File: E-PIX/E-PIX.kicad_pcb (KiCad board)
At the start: 2 copper layers, 40.1 x 45 mm, 65 parts, among them J1 USB_C_Receptacle_USB2.0, J2 DM3AT-SF-PEJM5, Q1 AO3401A, Q2 2SC4213, Q3 2SC4213, Q4 BSS138, Q5 BSS138, SW1 SW_Push, SW2 SW_Push, U10 ESP32-S3-WROOM-1, U2 NJM7805SDL1, U3 AZ1117-3.3, U4 BTS6142D, U5 Conn_03x02, U6 Conn_03x04, U7 U7, U8 U8, U9 FT231XS

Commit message: adjust all the footprints. start trying free routing
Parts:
- moved R14 1.27 mm to (140.2, 87.3)
- moved R19 1.27 mm to (144.0, 87.3)
- moved R4 1.27 mm to (147.8, 87.3)
- renumbered U1 to BNO055
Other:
- board text added: "CPU"
- board text added: "POWER"
- board text added: "VSS"
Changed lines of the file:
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@@
 		(tags "capacitor")
 		(property "Reference" "C11"
-			(at -1.7 1.905 180)
+			(at -1.7 2.54 180)
 			(layer "F.SilkS")
 			(effects
@@
 		(tags "USB C Type-C Receptacle SMD")
 		(property "Reference" "J1"
-			(at 4.57 -5.715 90)
+			(at 0.125 -5.715 90)
 			(layer "F.SilkS")
 			(effects
@@
 		(descr "PH-3X4SG")
 		(property "Reference" "U6"
-			(at -3.81 -1.27 0)
+			(at -3.175 -1.27 0)
 			(layer "F.SilkS")
 			(effects
@@
 		(tags "SSOP 0.635")
 		(property "Reference" "U9"
-			(at 5.02 -3.4925 180)
+			(at 3.75 -4.1275 180)
 			(layer "F.SilkS")
 			(effects
@@
 		(tags "DPAK TO-252 DPAK-5 TO-252-5")
 		(property "Reference" "U4"
-			(at -4.86 -0.001 90)
+			(at 2.76 4.825 0)
 			(layer "F.SilkS")
 			(effects
@@
 		(descr "PH-3X4SG")
 		(property "Reference" "U5"
-			(at -1.905 5.715 90)
+			(at -2.54 5.715 90)
 			(layer "F.SilkS")
 			(effects
@@
 		(tags "CP Radial series Radial pin pitch 3.50mm diameter 8mm height 12mm Electrolytic Capacitor")
 		(property "Reference" "C3"
-			(at 1.75 5.08 90)
+			(at -3.81 2.54 90)
 			(layer "F.SilkS")
 			(effects
@@
 		(tags "LED")
 		(property "Reference" "D9"
-			(at -3.0225 0 90)
+			(at 1.38 4.76 180)
 			(layer "B.SilkS")
 			(effects
 				(font
-					(size 1 1)
-					(thickness 0.15)
+					(size 0.6 0.6)
+					(thickness 0.075)
 				)
 				(justify mirror)
@@
 		(property "Value" "U7"
 			(at 1.85 0.026 0)
-			(layer "B.SilkS")
+			(layer "B.SilkS" knockout)
 			(effects
 				(font
 					(size 1 1)
-					(thickness 0.2)
+					(thickness 0.15)
 				)
 				(justify mirror)
@@
 		(layer "B.Cu")
 		(at 131.75 91.11 180)
-		(property "Reference" "U1"
-			(at 0 13 0)
+		(property "Reference" "BNO055"
+			(at 0 -10.16 0)
 			(unlocked yes)
 			(layer "B.SilkS")
@@
 				(font
 					(size 1 1)
-					(thickness 0.1)
+					(thickness 0.15)
 				)
 				(justify mirror)
@@
 		(tags "capacitor")
 		(property "Reference" "C7"
-			(at 2.225 0 90)
+			(at 1.59 0 90)
 			(layer "B.SilkS")
 			(effects
 				(font
-					(size 1 1)
-					(thickness 0.15)
+					(size 0.6 0.6)
+					(thickness 0.075)
 				)
 				(justify mirror)
@@
 		(tags "capacitor")
 		(property "Reference" "C9"
-			(at 3.315 0 90)
+			(at 1.05558 -1.905 180)
 			(layer "B.SilkS")
 			(effects
 				(font
-					(size 1 1)
-					(thickness 0.15)
+					(size 0.6 0.6)
+					(thickness 0.075)
 				)
 				(justify mirror)
@@
 	(footprint "Resistor_SMD:R_0603_1608Metric"
 		(layer "B.Cu")
-		(at 145.275 87.3 180)
+		(at 144.005 87.3 180)
 		(descr "Resistor SMD 0603 (1608 Metric), square (rectangular) end terminal, IPC-7351 nominal, (Body size source: IPC-SM-782 page 72, https://www.pcb-3d.com/wordpress/wp-content/uploads/ipc-sm-782a_amendment_1_and_2.pdf), generated with kicad-footprint-generator")
 		(tags "resistor")
 		(property "Reference" "R19"
-			(at 0 1.43 0)
+			(at 4.635 -2.54 0)
 			(layer "B.SilkS")
 			(effects
 				(font
-					(size 1 1)
-					(thickness 0.15)
+					(size 0.6 0.6)
+					(thickness 0.075)
 				)
 				(justify mirror)
@@
 		(tags "capacitor")
 		(property "Reference" "C8"
-			(at 2.225 0 90)
+			(at 1.59 0 90)
 			(layer "B.SilkS")
 			(effects
 				(font
-					(size 1 1)
-					(thickness 0.15)
+					(size 0.6 0.6)
+					(thickness 0.075)
 				)
 				(justify mirror)
@@
 		(tags "LED")
 		(property "Reference" "D4"
-			(at -3.0225 0 270)
+			(at -1.16 7.3 0)
 			(layer "B.SilkS")
 			(effects
 				(font
-					(size 1 1)
-					(thickness 0.15)
+					(size 0.6 0.6)
+					(thickness 0.075)
 				)
 				(justify mirror)
@@
 		(tags "capacitor")
 		(property "Reference" "C10"
-			(at 3.315 0 90)
+			(at 0.14 -4.445 180)
 			(layer "B.SilkS")
 			(effects
 				(font
-					(size 1 1)
-					(thickness 0.15)
+					(size 0.6 0.6)
+					(thickness 0.075)
 				)
 				(justify mirror)
@@
 		(tags "resistor")
 		(property "Reference" "R15"
-			(at 3.315 0 90)
+			(at 0.14 1.905 90)
 			(layer "B.SilkS")
 			(effects
@@
 	(footprint "Resistor_SMD:R_0603_1608Metric"
 		(layer "B.Cu")
-		(at 149.085 87.3 180)
+		(at 147.815 87.3 180)
 		(descr "Resistor SMD 0603 (1608 Metric), square (rectangular) end terminal, IPC-7351 nominal, (Body size source: IPC-SM-782 page 72, https://www.pcb-3d.com/wordpress/wp-content/uploads/ipc-sm-782a_amendment_1_and_2.pdf), generated with kicad-footprint-generator")
 		(tags "resistor")
 		(property "Reference" "R4"
-			(at 0 1.43 0)
+			(at 8.445 -1.27 0)
 			(layer "B.SilkS")
 			(effects
 				(font
-					(size 1 1)
-					(thickness 0.15)
+					(size 0.6 0.6)
+					(thickness 0.075)
 				)
 				(justify mirror)
@@
 	(footprint "Resistor_SMD:R_0603_1608Metric"
 		(layer "B.Cu")
-		(at 141.465 87.3 180)
+		(at 140.195 87.3 180)
 		(descr "Resistor SMD 0603 (1608 Metric), square (rectangular) end terminal, IPC-7351 nominal, (Body size source: IPC-SM-782 page 72, https://www.pcb-3d.com/wordpress/wp-content/uploads/ipc-sm-782a_amendment_1_and_2.pdf), generated with kicad-footprint-generator")
 		(tags "resistor")
 		(property "Reference" "R14"
-			(at 0 1.43 0)
+			(at 0.825 -3.81 0)
 			(layer "B.SilkS")
 			(effects
 				(font
-					(size 1 1)
-					(thickness 0.15)
+					(size 0.6 0.6)
+					(thickness 0.075)
 				)
 				(justify mirror)
@@
 				(font
 					(size 1 1)
-					(thickness 0.2)
+					(thickness 0.15)
 				)
 				(justify mirror)
@@
 		(tags "LED RGB NeoPixel PLCC-4 5050")
 		(property "Reference" "D6"
-			(at 4.765 0.125 0)
+			(at -4.76 2.03 0)
 			(layer "B.SilkS")
 			(effects
@@
 			(layer "B.Fab")
 		)
-		(fp_text user "1"
-			(at -4.15 1.6 0)
-			(layer "B.SilkS")
-			(effects
-				(font
-					(size 1 1)
-					(thickness 0.15)
-				)
-				(justify mirror)
-			)
-		)
 		(fp_text user "${REFERENCE}"
 			(at 0 0 0)
@@
 		(tags "LED")
 		(property "Reference" "D7"
-			(at -3.0225 0 90)
+			(at 0.11 2.22 180)
 			(layer "B.SilkS")
 			(effects
 				(font
-					(size 1 1)
-					(thickness 0.15)
+					(size 0.6 0.6)
+					(thickness 0.075)
 				)
 				(justify mirror)
@@
 		(layer "Edge.Cuts")
 	)
+	(gr_text "VSS"
+		(at 148.895 86.03 0)
+		(layer "B.SilkS")
+		(effects
+			(font
+				(size 0.6 0.6)
+				(thickness 0.075)
+			)
+			(justify left bottom mirror)
+		)
+	)
+	(gr_text "POWER"
+		(at 151.435 84.76 90)
+		(layer "B.SilkS")
+		(effects
+			(font
+				(size 1 1)
+				(thickness 0.15)
+			)
+			(justify left bottom mirror)
+		)
+	)
+	(gr_text "CPU"
+		(at 146.355 86.03 0)
+		(layer "B.SilkS")
+		(effects
+			(font
+				(size 0.6 0.6)
+				(thickness 0.075)
+			)
+			(justify left bottom mirror)
+		)
+	)
 	(embedded_fonts no)

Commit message: route main wires
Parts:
- R1: moved to F.Cu
- turned U9 to -90 degrees
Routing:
- net VSS: track 0.00 -> 41.2 mm, vias 0 -> 4
- net /ICS2_5V: track 0.00 -> 27.2 mm
- net /ICS1_5V: track 0.00 -> 17.8 mm
- net /CS: track 0.00 -> 16.9 mm, vias 0 -> 2
- net /MOSI: track 0.00 -> 15.4 mm, vias 0 -> 2
- net /CLK: track 0.00 -> 13.3 mm, vias 0 -> 2
- net /RX2: track 0.00 -> 12.4 mm, vias 0 -> 1
- net /TX2: track 0.00 -> 12.2 mm, vias 0 -> 1
- net /ICS2_3V3: track 0.00 -> 12.2 mm
- net /RX0: track 0.00 -> 11.9 mm
- net /ICS1_3V3: track 0.00 -> 11.7 mm
- net Net-(U4-IN): track 0.00 -> 10.8 mm
- net /MISO: track 0.00 -> 10.6 mm, vias 0 -> 2
- net /TX0: track 0.00 -> 10.0 mm
- net /TX1: track 0.00 -> 7.41 mm, vias 0 -> 1
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- added copper zone on F.Cu, net +3V3
- added copper zone on In1.Cu, net +3V3
- added copper zone on B.Cu, net GND
- added copper zone on F.Cu, net GND
- added copper zone on In1.Cu, net GND
- added copper zone on In2.Cu, net GND
- added copper zone on In3.Cu, net GND
- added copper zone on In4.Cu, net GND
- added copper zone on F.Cu, net VDD
- added copper zone on B.Cu, net VSS
- added copper zone on F.Cu, net VSS
- added copper zone on In1.Cu, net VSS
- added copper zone on In2.Cu, net VSS
- added copper zone on In3.Cu, net VSS
- added copper zone on In4.Cu, net VSS
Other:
- copper layers 2 -> 6

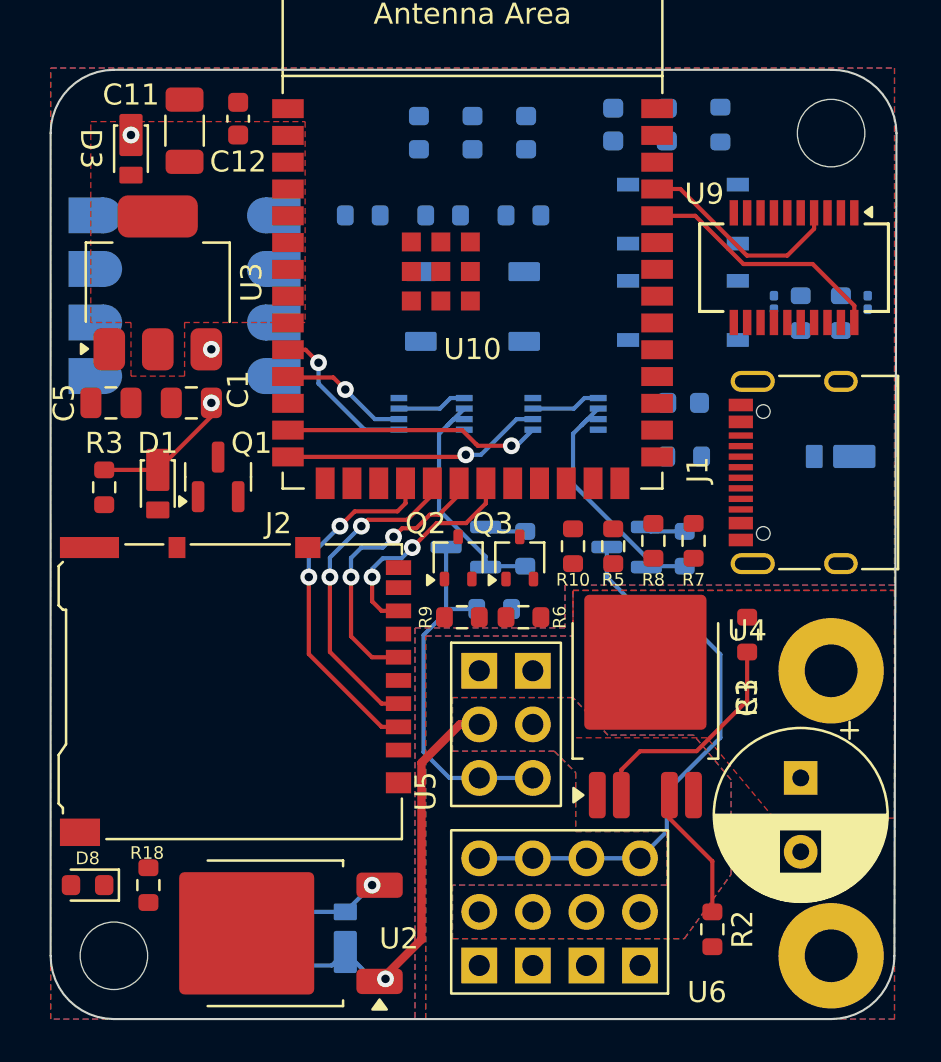
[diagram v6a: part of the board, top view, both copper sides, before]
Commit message: failed free routing
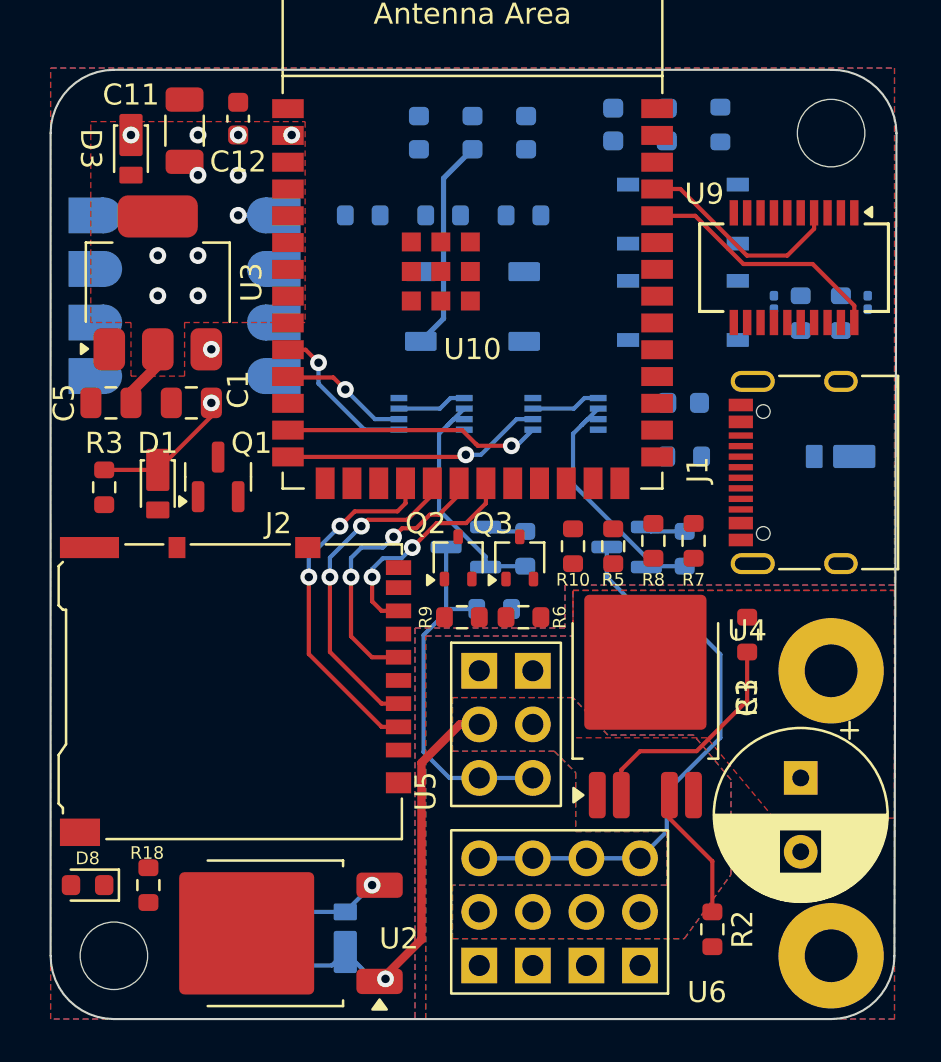
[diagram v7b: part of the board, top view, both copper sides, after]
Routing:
- net +3V3: track 3.87 -> 18.3 mm, vias 0 -> 10
- net VSS: track 41.2 -> 42.0 mm

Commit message: move some tips
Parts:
- C1, C5, D1, Q1, Q2, Q3, R10, R3, R5, R6, R7, R8, R9: moved to B.Cu
- C7, C8, Q4, Q5, R12, R13, R16, R17, R20, R21: moved to F.Cu
- U7: value U7 -> TC7WH241FK; moved to F.Cu
- U8: value U8 -> TC7WH241FK; moved to F.Cu
- moved R3 17.6 mm to (130.5, 82.7), turned to 0 degrees
- moved U8 17.6 mm to (132.4, 99.0), turned to 0 degrees
- moved U7 15.7 mm to (127.9, 99.0), turned to 0 degrees
- moved Q1 15.4 mm to (133.0, 84.3), turned to 180 degrees
- moved D1 14.2 mm to (130.0, 85.8), turned to 90 degrees
- moved R6 11.1 mm to (143.4, 96.2)
- moved R12 9.34 mm to (156.1, 99.9)
- moved R5 8.25 mm to (147.4, 96.2), turned to 180 degrees
- moved R13 8.07 mm to (156.1, 96.4)
- moved C8 7.71 mm to (156.8, 93.9), turned to 0 degrees
- moved U1 7.62 mm to (131.8, 98.7)
- moved R10 6.97 mm to (143.4, 101.3), turned to 0 degrees
- moved C1 5.86 mm to (132.5, 90.3), turned to -90 degrees
- moved C5 5.85 mm to (127.9, 90.3), turned to 90 degrees
- moved R9 5.66 mm to (147.4, 101.3)
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- renumbered BNO055 to U1
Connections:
- U10 pad 15: unconnected-(U10-IO3-Pad15) -> /EN2
- U10 pad 22: /EN1 -> unconnected-(U10-IO14-Pad22)
- U10 pad 23: /EN2 -> unconnected-(U10-IO21-Pad23)
- U10 pad 28: /SW -> unconnected-(U10-IO35-Pad28)
- U10 pad 31: unconnected-(U10-IO38-Pad31) -> /SW
- U10 pad 9: unconnected-(U10-IO16-Pad9) -> /EN1
- U5 pad 3: /ICS1_5V -> /ICS2_5V
- U6 pad 3: /ICS2_5V -> /ICS1_5V
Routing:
- net VSS: track 42.0 -> 8.08 mm, vias 4 -> 2
- net /CS: track 16.9 -> 0.00 mm, vias 2 -> 0
- net /MOSI: track 15.4 -> 0.00 mm, vias 2 -> 0
- net +3V3: track 18.3 -> 3.66 mm, vias 10 -> 1
- net /CLK: track 13.3 -> 0.00 mm, vias 2 -> 0
- net /ICS2_3V3: track 12.2 -> 25.2 mm
- net Net-(U9-USBDM): track 0.00 -> 12.3 mm
- net /EN1: track 3.31 -> 15.0 mm
- net /MISO: track 10.6 -> 0.00 mm, vias 2 -> 0
- net /TX2: track 12.2 -> 3.52 mm, vias 1 -> 0
- net /ICS1_3V3: track 11.7 -> 20.2 mm
- net /EN2: track 3.31 -> 11.1 mm
- net /RX2: track 12.4 -> 4.96 mm, vias 1 -> 0
- net /ICS1_5V: track 18.0 -> 25.0 mm
- net Net-(U4-IS): track 6.38 -> 0.00 mm
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- added copper zone on B.Cu, net +3V3
- added copper zone on In2.Cu, net +3V3
- added copper zone on In3.Cu, net +3V3
- added copper zone on In4.Cu, net +3V3
